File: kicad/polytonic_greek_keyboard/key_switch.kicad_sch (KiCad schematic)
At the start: 2 parts, among them SW3 SW_SPST

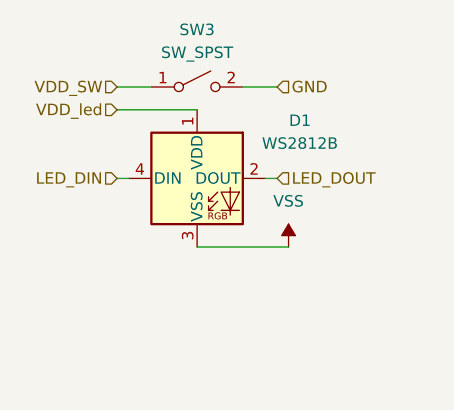
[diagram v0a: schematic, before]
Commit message: [ADD] an initial matrix of what the keyboard will look like logically
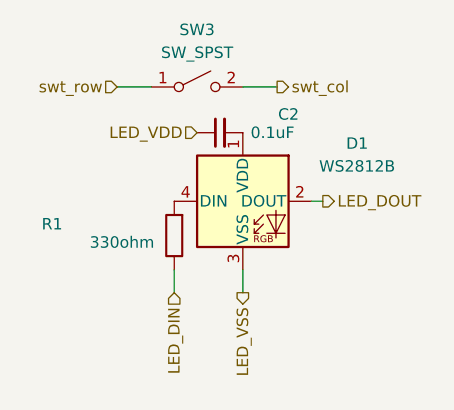
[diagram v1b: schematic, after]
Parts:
- added C2: 0.1uF_0603_16V, 4ms_Capacitor:C_0603, symbol PCM_4ms_Capacitor:0.1uF_0603_16V
- added R1: 330ohm, Resistor_THT:R_Axial_DIN0207_L6.3mm_D2.5mm_P10.16mm_Horizontal, symbol PCM_SL_Resistors:330ohm
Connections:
- net LED_DIN: now also R1.2; no longer D1.4 (DIN)
- net GND renamed swt_col
- net VDD_SW renamed swt_row
- net VDD_led: no longer names the net of D1.1 (VDD)
- net VDD_led: now also C2.2
- net VSS renamed LED_VSS
- new net: D1.4 (DIN), R1.1
- new net LED_VDD: C2.1
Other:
- moved on the sheet: D1

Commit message: [ADD] a more structured approach of the pcb in a way that won't overload the esp32 that is running it
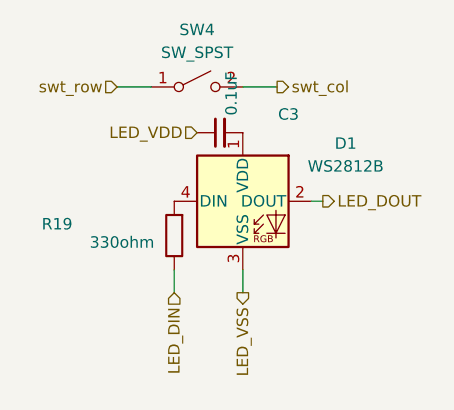
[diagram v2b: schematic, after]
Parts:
- C3: renamed from C2; footprint 4ms_Capacitor:C_0603 -> Capacitor_SMD:C_0201_0603Metric
- renumbered R1 to R19, SW3 to SW4
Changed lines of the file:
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@@
 		(fields_autoplaced yes)
 		(property "Reference" "D1"
-			(at 50.8 26.5998 0)
+			(at 49.53 26.5998 0)
 			(effects
 				(font
@@
 		)
 		(property "Value" "WS2812B"
-			(at 50.8 29.1398 0)
+			(at 49.53 29.1398 0)
 			(effects
 				(font
@@
 				)
 				(path "/cbe25a1b-6c02-43c2-9ff9-ba274c7cf6a2/09ff75ff-3c8b-43b7-a704-ac023cbe9eff/5f107f1d-b7cf-41cd-afd8-8e41c5a88225"
-					(reference "D1")
+					(reference "D4")
 					(unit 1)
 				)
 				(path "/cbe25a1b-6c02-43c2-9ff9-ba274c7cf6a2/09ff75ff-3c8b-43b7-a704-ac023cbe9eff/6fe76989-dc92-4d30-a709-538a22e097b7"
-					(reference "D1")
+					(reference "D2")
 					(unit 1)
 				)
 				(path "/cbe25a1b-6c02-43c2-9ff9-ba274c7cf6a2/09ff75ff-3c8b-43b7-a704-ac023cbe9eff/85dfdcb0-9a07-4e64-aafd-2caa92dd5075"
-					(reference "D1")
+					(reference "D3")
 					(unit 1)
 				)
@@
 		(dnp no)
 		(fields_autoplaced yes)
-		(property "Reference" "SW3"
+		(property "Reference" "SW4"
 			(at 33.02 13.97 0)
 			(effects
@@
 			(project "polytonic_greek_keyboard"
 				(path "/cbe25a1b-6c02-43c2-9ff9-ba274c7cf6a2/09ff75ff-3c8b-43b7-a704-ac023cbe9eff/0a734353-c161-4bd5-883e-eaf92a492627"
-					(reference "SW3")
+					(reference "SW4")
 					(unit 1)
 				)
 				(path "/cbe25a1b-6c02-43c2-9ff9-ba274c7cf6a2/09ff75ff-3c8b-43b7-a704-ac023cbe9eff/5f107f1d-b7cf-41cd-afd8-8e41c5a88225"
-					(reference "SW3")
+					(reference "SW7")
 					(unit 1)
 				)
 				(path "/cbe25a1b-6c02-43c2-9ff9-ba274c7cf6a2/09ff75ff-3c8b-43b7-a704-ac023cbe9eff/6fe76989-dc92-4d30-a709-538a22e097b7"
-					(reference "SW3")
+					(reference "SW5")
 					(unit 1)
 				)
 				(path "/cbe25a1b-6c02-43c2-9ff9-ba274c7cf6a2/09ff75ff-3c8b-43b7-a704-ac023cbe9eff/85dfdcb0-9a07-4e64-aafd-2caa92dd5075"
-					(reference "SW3")
+					(reference "SW6")
 					(unit 1)
 				)
@@
 		(on_board yes)
 		(dnp no)
-		(property "Reference" "C2"
+		(property "Reference" "C3"
 			(at 43.18 23.368 90)
 			(effects
@@
 			)
 		)
-		(property "Footprint" "4ms_Capacitor:C_0603"
+		(property "Footprint" "Capacitor_SMD:C_0201_0603Metric"
 			(at 40.64 27.94 0)
 			(effects
@@
 		)
 		(property "Display" "0.1uF"
-			(at 41.402 25.4 90)
-			(effects
-				(font
-					(size 1.27 1.27)
-				)
+			(at 36.83 23.495 0)
+			(effects
+				(font
+					(size 1.27 1.27)
+				)
+				(justify left)
 			)
 		)
@@
 			(project "polytonic_greek_keyboard"
 				(path "/cbe25a1b-6c02-43c2-9ff9-ba274c7cf6a2/09ff75ff-3c8b-43b7-a704-ac023cbe9eff/0a734353-c161-4bd5-883e-eaf92a492627"
-					(reference "C2")
+					(reference "C3")
 					(unit 1)
 				)
 				(path "/cbe25a1b-6c02-43c2-9ff9-ba274c7cf6a2/09ff75ff-3c8b-43b7-a704-ac023cbe9eff/5f107f1d-b7cf-41cd-afd8-8e41c5a88225"
-					(reference "C2")
+					(reference "C8")
 					(unit 1)
 				)
 				(path "/cbe25a1b-6c02-43c2-9ff9-ba274c7cf6a2/09ff75ff-3c8b-43b7-a704-ac023cbe9eff/6fe76989-dc92-4d30-a709-538a22e097b7"
-					(reference "C2")
+					(reference "C4")
 					(unit 1)
 				)
 				(path "/cbe25a1b-6c02-43c2-9ff9-ba274c7cf6a2/09ff75ff-3c8b-43b7-a704-ac023cbe9eff/85dfdcb0-9a07-4e64-aafd-2caa92dd5075"
-					(reference "C2")
+					(reference "C5")
 					(unit 1)
 				)
@@
 		(on_board yes)
 		(dnp no)
-		(property "Reference" "R1"
+		(property "Reference" "R19"
 			(at 15.748 35.56 90)
 			(effects
@@
 			(project "polytonic_greek_keyboard"
 				(path "/cbe25a1b-6c02-43c2-9ff9-ba274c7cf6a2/09ff75ff-3c8b-43b7-a704-ac023cbe9eff/0a734353-c161-4bd5-883e-eaf92a492627"
-					(reference "R1")
+					(reference "R19")
 					(unit 1)
 				)
 				(path "/cbe25a1b-6c02-43c2-9ff9-ba274c7cf6a2/09ff75ff-3c8b-43b7-a704-ac023cbe9eff/5f107f1d-b7cf-41cd-afd8-8e41c5a88225"
-					(reference "R1")
+					(reference "R23")
 					(unit 1)
 				)
 				(path "/cbe25a1b-6c02-43c2-9ff9-ba274c7cf6a2/09ff75ff-3c8b-43b7-a704-ac023cbe9eff/6fe76989-dc92-4d30-a709-538a22e097b7"
-					(reference "R1")
+					(reference "R20")
 					(unit 1)
 				)
 				(path "/cbe25a1b-6c02-43c2-9ff9-ba274c7cf6a2/09ff75ff-3c8b-43b7-a704-ac023cbe9eff/85dfdcb0-9a07-4e64-aafd-2caa92dd5075"
-					(reference "R1")
-					(unit 1)
-				)
+					(reference "R21")
+					(unit 1)
+				)

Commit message: [UPDATE] the board desing, [FIX] connection issues
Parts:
- C3: footprint Capacitor_SMD:C_0201_0603Metric -> Capacitor_SMD:C_0201_0603Metric_Pad0.64x0.40mm_HandSolder
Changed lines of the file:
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@@
 			)
 		)
-		(property "Footprint" "Capacitor_SMD:C_0201_0603Metric"
+		(property "Footprint" "Capacitor_SMD:C_0201_0603Metric_Pad0.64x0.40mm_HandSolder"
 			(at 40.64 27.94 0)
 			(effects

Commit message: [UPDATE] anotation issues
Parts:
- renumbered C3 to C6, D1 to D5, R19 to R26, SW4 to SW6
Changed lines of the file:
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@@
 		(dnp no)
 		(fields_autoplaced yes)
-		(property "Reference" "D1"
+		(property "Reference" "D5"
 			(at 49.53 26.5998 0)
 			(effects
@@
 			(project "polytonic_greek_keyboard"
 				(path "/cbe25a1b-6c02-43c2-9ff9-ba274c7cf6a2/dc7dc8d0-3fc1-4401-9905-7f0a56042fcf/3567022d-dcc8-4a26-83e7-5efb883a1646/0a734353-c161-4bd5-883e-eaf92a492627"
-					(reference "D1")
+					(reference "D5")
 					(unit 1)
 				)
 				(path "/cbe25a1b-6c02-43c2-9ff9-ba274c7cf6a2/dc7dc8d0-3fc1-4401-9905-7f0a56042fcf/3567022d-dcc8-4a26-83e7-5efb883a1646/5f107f1d-b7cf-41cd-afd8-8e41c5a88225"
-					(reference "D2")
+					(reference "D6")
 					(unit 1)
 				)
 				(path "/cbe25a1b-6c02-43c2-9ff9-ba274c7cf6a2/dc7dc8d0-3fc1-4401-9905-7f0a56042fcf/3567022d-dcc8-4a26-83e7-5efb883a1646/6fe76989-dc92-4d30-a709-538a22e097b7"
-					(reference "D3")
+					(reference "D7")
 					(unit 1)
 				)
 				(path "/cbe25a1b-6c02-43c2-9ff9-ba274c7cf6a2/dc7dc8d0-3fc1-4401-9905-7f0a56042fcf/3567022d-dcc8-4a26-83e7-5efb883a1646/85dfdcb0-9a07-4e64-aafd-2caa92dd5075"
-					(reference "D4")
+					(reference "D8")
 					(unit 1)
 				)
@@
 		(dnp no)
 		(fields_autoplaced yes)
-		(property "Reference" "SW4"
+		(property "Reference" "SW6"
 			(at 33.02 13.97 0)
 			(effects
@@
 			(project "polytonic_greek_keyboard"
 				(path "/cbe25a1b-6c02-43c2-9ff9-ba274c7cf6a2/dc7dc8d0-3fc1-4401-9905-7f0a56042fcf/3567022d-dcc8-4a26-83e7-5efb883a1646/0a734353-c161-4bd5-883e-eaf92a492627"
-					(reference "SW4")
+					(reference "SW6")
 					(unit 1)
 				)
 				(path "/cbe25a1b-6c02-43c2-9ff9-ba274c7cf6a2/dc7dc8d0-3fc1-4401-9905-7f0a56042fcf/3567022d-dcc8-4a26-83e7-5efb883a1646/5f107f1d-b7cf-41cd-afd8-8e41c5a88225"
-					(reference "SW5")
+					(reference "SW7")
 					(unit 1)
 				)
 				(path "/cbe25a1b-6c02-43c2-9ff9-ba274c7cf6a2/dc7dc8d0-3fc1-4401-9905-7f0a56042fcf/3567022d-dcc8-4a26-83e7-5efb883a1646/6fe76989-dc92-4d30-a709-538a22e097b7"
-					(reference "SW6")
+					(reference "SW8")
 					(unit 1)
 				)
 				(path "/cbe25a1b-6c02-43c2-9ff9-ba274c7cf6a2/dc7dc8d0-3fc1-4401-9905-7f0a56042fcf/3567022d-dcc8-4a26-83e7-5efb883a1646/85dfdcb0-9a07-4e64-aafd-2caa92dd5075"
-					(reference "SW7")
+					(reference "SW9")
 					(unit 1)
 				)
@@
 		(on_board yes)
 		(dnp no)
-		(property "Reference" "C3"
+		(property "Reference" "C6"
 			(at 43.18 23.368 90)
 			(effects
@@
 			(project "polytonic_greek_keyboard"
 				(path "/cbe25a1b-6c02-43c2-9ff9-ba274c7cf6a2/dc7dc8d0-3fc1-4401-9905-7f0a56042fcf/3567022d-dcc8-4a26-83e7-5efb883a1646/0a734353-c161-4bd5-883e-eaf92a492627"
-					(reference "C3")
+					(reference "C6")
 					(unit 1)
 				)
 				(path "/cbe25a1b-6c02-43c2-9ff9-ba274c7cf6a2/dc7dc8d0-3fc1-4401-9905-7f0a56042fcf/3567022d-dcc8-4a26-83e7-5efb883a1646/5f107f1d-b7cf-41cd-afd8-8e41c5a88225"
-					(reference "C4")
+					(reference "C7")
 					(unit 1)
 				)
 				(path "/cbe25a1b-6c02-43c2-9ff9-ba274c7cf6a2/dc7dc8d0-3fc1-4401-9905-7f0a56042fcf/3567022d-dcc8-4a26-83e7-5efb883a1646/6fe76989-dc92-4d30-a709-538a22e097b7"
-					(reference "C5")
+					(reference "C8")
 					(unit 1)
 				)
 				(path "/cbe25a1b-6c02-43c2-9ff9-ba274c7cf6a2/dc7dc8d0-3fc1-4401-9905-7f0a56042fcf/3567022d-dcc8-4a26-83e7-5efb883a1646/85dfdcb0-9a07-4e64-aafd-2caa92dd5075"
-					(reference "C8")
+					(reference "C9")
 					(unit 1)
 				)
@@
 		(on_board yes)
 		(dnp no)
-		(property "Reference" "R19"
+		(property "Reference" "R26"
 			(at 15.748 35.56 90)
 			(effects
@@
 			(project "polytonic_greek_keyboard"
 				(path "/cbe25a1b-6c02-43c2-9ff9-ba274c7cf6a2/dc7dc8d0-3fc1-4401-9905-7f0a56042fcf/3567022d-dcc8-4a26-83e7-5efb883a1646/0a734353-c161-4bd5-883e-eaf92a492627"
-					(reference "R19")
+					(reference "R26")
 					(unit 1)
 				)
 				(path "/cbe25a1b-6c02-43c2-9ff9-ba274c7cf6a2/dc7dc8d0-3fc1-4401-9905-7f0a56042fcf/3567022d-dcc8-4a26-83e7-5efb883a1646/5f107f1d-b7cf-41cd-afd8-8e41c5a88225"
-					(reference "R20")
+					(reference "R27")
 					(unit 1)
 				)
 				(path "/cbe25a1b-6c02-43c2-9ff9-ba274c7cf6a2/dc7dc8d0-3fc1-4401-9905-7f0a56042fcf/3567022d-dcc8-4a26-83e7-5efb883a1646/6fe76989-dc92-4d30-a709-538a22e097b7"
-					(reference "R21")
+					(reference "R28")
 					(unit 1)
 				)
 				(path "/cbe25a1b-6c02-43c2-9ff9-ba274c7cf6a2/dc7dc8d0-3fc1-4401-9905-7f0a56042fcf/3567022d-dcc8-4a26-83e7-5efb883a1646/85dfdcb0-9a07-4e64-aafd-2caa92dd5075"
-					(reference "R23")
-					(unit 1)
-				)
+					(reference "R29")
+					(unit 1)
+				)

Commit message: [UPDATE] the final merged version of the schematic before splitting into two separate kicad projects
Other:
- company: (none) -> Henry's Software House
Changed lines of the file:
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@@
 	(generator_version "9.0")
 	(paper "A4")
+	(title_block
+		(rev "1 - do not edit connector pin layout.")
+		(company "Henry's Software House")
+	)
 	(wire
 		(pts
